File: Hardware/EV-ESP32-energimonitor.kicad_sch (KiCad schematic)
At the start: 0 parts

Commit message: HW added
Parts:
- added A1: ESP32_DevKit_V1_DOIT, Local_MCU_Module_Library:esp32_devkit_v1_doit (F.Mount), symbol Local_MCU_Module_Library:ESP32_DevKit_V1_DOIT
- added A2: DC-DC 3.3V 3A, Local_Misckllaneous_Library:DC-DC_3.3V_3A_Stepdown (F.Mount), symbol Local_Miscellaneous_Library:DC-DC_Step_Down_3.3V_3A
- added F1: Fuse, symbol Device:Fuse
- added J1: Conn_01x04_Socket, symbol Connector:Conn_01x04_Socket
- added PS1: RAC04-05SGA, Converter_ACDC:Converter_ACDC_RECOM_RAC04-xxSGx_THT, symbol Converter_ACDC:RAC04-05SGA
- added RV1: Varistor, symbol Device:Varistor

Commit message: HW: diagram added
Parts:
- removed J1: Conn_01x04_Socket, symbol Connector:Conn_01x04_Socket
- added C1, C7: C10uf, Capacitor_SMD:C_0603_1608Metric, symbol Local_Device_Library:C10uf
- added C2, C3, C4, C5, C6, C8: C100nf, Capacitor_SMD:C_0402_1005Metric, symbol Local_Device_Library:C100nf
- added C9: C, symbol Device:C
- added J2: Conn_01x02_Pin, symbol Connector:Conn_01x02_Pin
- added J3: RJ22, symbol Connector:RJ22
- added Q1: PNP, symbol Simulation_SPICE:PNP
- added Q2, Q3: NPN, symbol Simulation_SPICE:NPN
- added R1, R2: R10K, Resistor_SMD:R_0402_1005Metric, symbol Local_Device_Library:R10K
- added R3, R9: R, symbol Device:R
- added R4, R5, R6, R7, R8: R4.7K, Resistor_SMD:R_0402_1005Metric, symbol Local_Device_Library:R4.7K
- added SW1, SW2, SW3, SW4: SW_Push, symbol Switch:SW_Push
- added SW2: SW_MEC_5E, symbol Switch:SW_MEC_5E
- added U1: ER_OLEDM0.91_1x-I2C, Display:ER_OLEDM0.91_1x-I2C, symbol Display_Graphic:ER_OLEDM0.91_1x-I2C
- added U2: 74HC14, Package_SO:SOIC-14_3.9x8.7mm_P1.27mm, symbol Local_Miscellaneous_Library:74HC14-local_74HCxx
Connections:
- net at PS1.1 (AC(L)): now also F1.1, RV1.1
- net at PS1.2 (AC(N)): now also RV1.2
- net GND1: now reaches PS1.4 (-Vout)
- net GND1: now also A2.3 (IN-), C9.2, Q2.3 (E), Q3.3 (E), SW2.3 (K), SW2.4 (A)
- net at PS1.5 (+Vout): now also Q1.3 (E), R3.1, R9.1
- net at A2.2 (IN+): now also Q1.1 (C)
- net -3V3: now reaches A2.5 (OUT+)
- net -3V3: now also A1.16 (3V3), C3.1, C4.1, C5.1, C6.1, C7.1, C8.1, R1.1, R4.1, SW1.2, SW2.2, SW3.2, SW4.2, U1.2 (VCC)
- net GND: now reaches A2.8 (OUT-)
- net GND: now also A1.14 (GND), A1.17 (GND), C1.2, C2.2, C7.2, C8.2, J3.2, R2.2, R5.2, R6.2, R7.2, R8.2, U1.1 (GND)
- net at A1.10 (IO27_(pullup)): now also U2.10
- net at A1.11 (IO14_(pullup)): now also U2.4
- net at A1.26 (IO21): now also U1.4 (SDA)
- net at A1.29 (IO22): now also U1.3 (SCL)
- net at A1.4 (IO34_(no_pullup)): now also J2.1 (Pin_1)
- net at A1.7 (IO33): now also U2.2
- net at A1.8 (IO25_(pullup)): now also U2.6
- net at A1.9 (IO26_(pullup)): now also U2.8
- new net: Q1.2 (B), Q2.1 (C), R3.2
- new net: C5.2, R7.1, SW3.1, U2.9
- new net: C9.1, Q2.2 (B), Q3.1 (C), R9.2, SW2.1, SW2.2
- new net: C4.2, R6.1, SW2.1, U2.5
- new net: C1.1, J2.2 (Pin_2), R1.2, R2.1
- new net: C3.2, R5.1, SW1.1, U2.3
- new net: C2.1, J3.3, R4.2, U2.1
- new net: C6.2, R8.1, SW4.1, U2.11
- no-connect marks 0 -> 4
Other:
- note added: "Connect to open collector output"
- note added: "EV charging start/stop"
- note added: "Keep near ESP32 pin 16"
- note added: "SCT01-T10/50A current sensor"
- note added: "price-limit decrease"
- note added: "price-limit increase"
- note added: "smart charging on/off"
- moved on the sheet: A2, F1, PS1, RV1

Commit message: HW: buttons, display and reboot logic added
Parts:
- removed A2: DC-DC 3.3V 3A, Local_Misckllaneous_Library:DC-DC_3.3V_3A_Stepdown (F.Mount), symbol Local_Miscellaneous_Library:DC-DC_Step_Down_3.3V_3A
- removed Q1: PNP, symbol Simulation_SPICE:PNP
- removed Q2, Q3: NPN, symbol Simulation_SPICE:NPN
- removed R9: R, symbol Device:R
- added C1, C11: 100n, symbol Device:C
- added C10: C_Polarized, symbol Device:C_Polarized
- added C2: 100nf, Capacitor_SMD:C_0402_1005Metric, symbol Local_Device_Library:C10nf
- added C3: 1uF, symbol Device:C
- added C4: 47nf, Capacitor_SMD:C_0402_1005Metric, symbol Local_Device_Library:C10nf
- added C5: 10uF, symbol Device:C
- added D1, D2, D3, D4: 1N4148WS, Diode_SMD:D_SOD-323F, symbol Local_Diode_Library:1N4148WS
- added D1, D2: LED_0805_G, LED_SMD:LED_0805_2012Metric, symbol Local_Diode_Library:LED_0805_G
- added J1: Screw_Terminal_01x02, symbol Connector:Screw_Terminal_01x02
- added J4: Conn_01x01_Pin, symbol Connector:Conn_01x01_Pin
- added J5, J6, J7, J8: Conn_01x06_Pin, symbol Connector:Conn_01x06_Pin
- added Q1, Q11, Q8: BC547, Package_TO_SOT_THT:TO-92_Inline, symbol Transistor_BJT:BC547
- added Q10: AO3401A, Package_TO_SOT_SMD:SOT-23, symbol Transistor_FET:AO3401A
- added Q2: IRF4905, Package_TO_SOT_THT:TO-220-3_Vertical, symbol Transistor_FET:IRF4905
- added Q4, Q5, Q6, Q7: S8050_NPN, Package_TO_SOT_SMD:SOT-23, symbol Local_Transistor_BJT_Library:S8050_NPN
- added Q9: NPN, symbol Simulation_SPICE:NPN
- added R1: 47K, symbol Device:R
- added R10, R13: R180, Resistor_SMD:R_0805_2012Metric, symbol Local_Device_Library:R180
- added R11, R12: R10K, Resistor_SMD:R_0402_1005Metric, symbol Local_Device_Library:R10K
- added R19, R6: 2,2K, symbol Device:R
- added R2: 68K, symbol Device:R
- added R20, R4, R7 (x2): 100K, symbol Device:R
- added R23: R, symbol Device:R
- added R3: 220K, symbol Device:R
- added R5: 330K -> 390K, symbol Device:R
- added R6: R4.7K, Resistor_SMD:R_0402_1005Metric, symbol Local_Device_Library:R4.7K
- added unit 2 of U1
- added unit 3 of U1
- added U5: 74HC14, Package_SO:SOIC-14_3.9x8.7mm_P1.27mm, symbol Local_Miscellaneous_Library:74HC14-local_74HCxx
- C9: value C -> 1uF
- R3: value R -> 100K
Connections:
- net GND: now also C9.2, PS1.4 (-Vout), C1.2, C10.2, C11.2, C3.2, C5.2, D1.2 (A), D4.2 (A), J8.4 (Pin_4), Q1.3 (E), Q11.3 (E), Q4.2 (E), Q6.2 (E), Q8.3 (E), Q9.3 (E), R10.2, R13.2, R3.2, R4.2, R7.2, R7.2, U5.7 (GND); no longer U1.1 (GND)
- net GND1: now also U1.1 (GND), J7.4 (Pin_4); no longer C9.2, PS1.4 (-Vout)
- net at PS1.5 (+Vout), R3.1: now also D3.1 (K), Q2.3 (S), R1.1, R19.2, R2.1, R5.1
- net at R3.2: now also Q1.1 (C), Q2.1 (G)
- net at PS1.2 (AC(N)), RV1.2: now also J1.2 (Pin_2)
- net at C5.2, R7.1, U2.9: now also J6.3 (Pin_3); no longer SW3.1
- net at F1.2: now also J1.1 (Pin_1)
- net HARD_RESET_GPIO: now reaches A1.13 (IO13_(pullup))
- net HARD_RESET_GPIO: now also R23.1
- net VCC: now reaches A1.15 (VIN)
- net VCC: now also C10.1, Q2.2 (D)
- net ext. LED1: now reaches A1.19 (IO2_/_LED_PIN)
- net ext. LED1: now also R11.1
- net OLED Touch: now reaches A1.20 (IO4_(pullup))
- net OLED Touch: now also J6.5 (Pin_5)
- net ext. LED2: now reaches A1.21 (IO16)
- net ext. LED2: now also R12.1
- net at U1.4 (SDA): now also J7.3 (Pin_3); no longer A1.26 (IO21)
- net at U1.3 (SCL): now also J7.2 (Pin_2); no longer A1.29 (IO22)
- net Direct Reset GPIO: now reaches A1.6 (IO32)
- net Direct Reset GPIO: now also Q11.1 (C)
- net at SW2.1, SW2.2: now also J5.6 (Pin_6); no longer C9.1
- net at C4.2, R6.1, U2.5: now also J6.2 (Pin_2); no longer SW2.1
- net at C3.2, R5.1, U2.3: now also J6.1 (Pin_1); no longer SW1.1
- net at C6.2, R8.1, U2.11: now also J6.4 (Pin_4); no longer SW4.1
- net +3.3V: now reaches U2.14 (VCC)
- net +3.3V: now also A1.16 (3V3), C3.1, C4.1, C5.1, C6.1, C7.1, C8.1, R1.1, R4.1, J8.1 (Pin_1)
- removed net -3V3: A1.16 (3V3), C3.1, C4.1, C5.1, C6.1, C7.1, C8.1, R1.1, R4.1, SW1.2, SW2.2, SW3.2, SW4.2, U1.2 (VCC)
- new net: Q6.1 (B), Q7.2 (E), R13.1
- new net: Q8.2 (B), R6.1, R7.1
- new net: Q1.2 (B), R6.2, R7.1
- new net: Q4.1 (B), Q5.2 (E), R10.1
- new net: Q4.3 (C), Q5.1 (B), R11.2
- new net: J5.2 (Pin_2), SW2.1
- new net: Q11.2 (B), R19.1, R20.1
- new net: Q6.3 (C), Q7.1 (B), R12.2
- new net: J8.5 (Pin_5), Q5.3 (C)
- new net: J5.3 (Pin_3), SW3.1
- new net: J5.4 (Pin_4), SW4.1
- new net: C11.1, C9.1, U5.14 (VCC)
- new net: J5.1 (Pin_1), SW1.1
- new net: J8.6 (Pin_6), Q7.3 (C)
- new net: D2.1 (K), J7.6 (Pin_6)
- new net: D1.1 (K), J7.5 (Pin_5)
- new net: J4.1 (Pin_1), J5.5 (Pin_5)
- new net: Q9.2 (B), R23.2
- new net +3.3VA: D1.2 (A), D2.2 (A), J7.1 (Pin_1), SW1.2, SW2.2, SW3.2, SW4.2, U1.2 (VCC)
- new net BASE_H: R6.1, U5.12
- new net DLY_H: C4.2, U1.4
- new net EDGE_H: D2.2 (A), U1.2
- new net Kill Switch: C1.1, C2.2, J6.6 (Pin_6), Q9.1 (C), R1.2
- new net N250: C3.1, D2.1 (K), R3.1, U1.3
- new net N3S: C5.1, Q8.1 (C), R5.2, U5.11
- new net NSTART: C4.1, D3.2 (A), D4.1 (K), R4.1, U1.5
- new net NTRIG: C2.1, D1.1 (K), R2.2, U1.1
- new net OFF_WIN_H: U5.10, U5.13
- new net SCL: A1.29 (IO22), J8.2 (Pin_2)
- new net SDA: A1.26 (IO21), J8.3 (Pin_3)
- new net START_H: R6.2, U5.8
- new net START_N: R20.2, U1.6, U5.9
- no-connect marks 4 -> 0
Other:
- note added: "Capasitor sensor"
- note added: "Input - Internal Pullup Trigger on Falling adge"
- note added: "Keep close to Pin 14"
- note added: "en ny version specifikt med 74HC14"
- moved on the sheet: A1, C1, C2, C3, C4, C5, C6, C7, C8, F1, J2, J3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

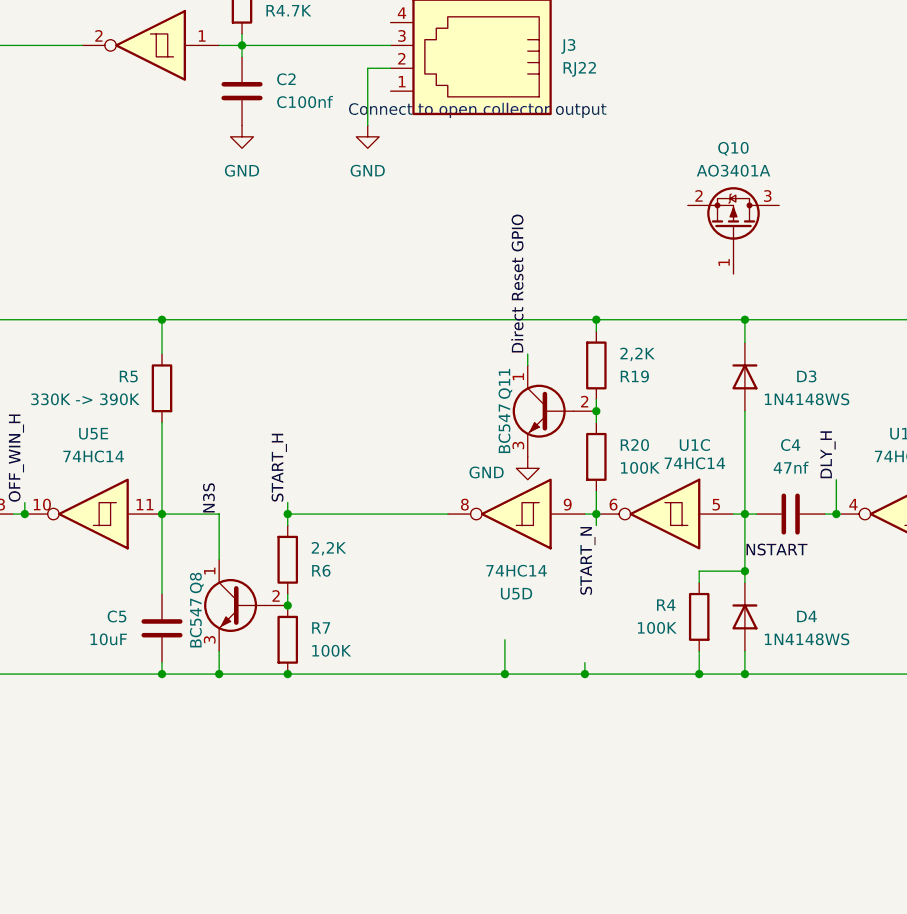
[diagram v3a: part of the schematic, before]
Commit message: FRM: #14 initial implementation. HW: Direct Reset GPIO Open Collector output added
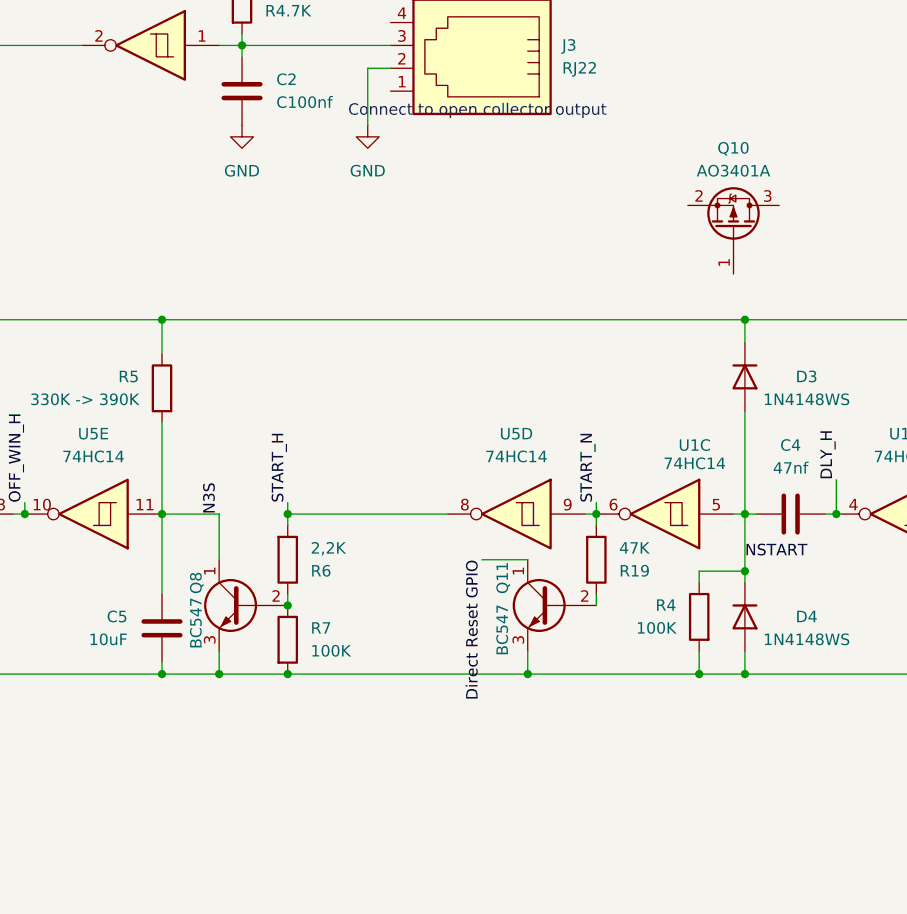
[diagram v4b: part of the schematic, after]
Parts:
- removed R20: 100K, symbol Device:R
- R19: value 2,2K -> 47K
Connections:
- net START_N: now also R19.2
- net at D3.1 (K), PS1.5 (+Vout), Q2.3 (S)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: no longer R19.2
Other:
- moved on the sheet: Q11, R19, U5D

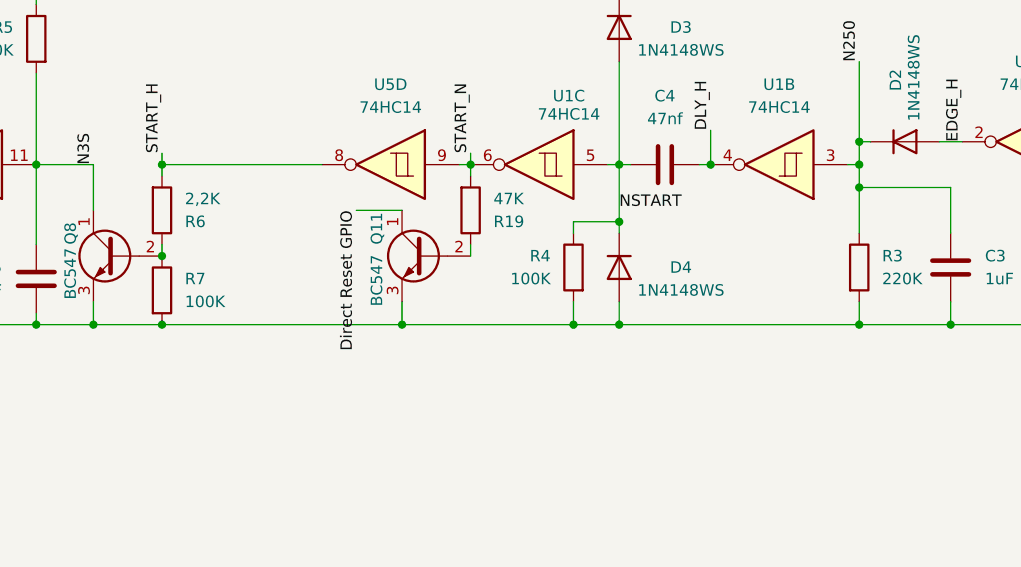
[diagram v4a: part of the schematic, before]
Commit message: HW: Direct Reset GPIO trigger moved to U1B pin 4
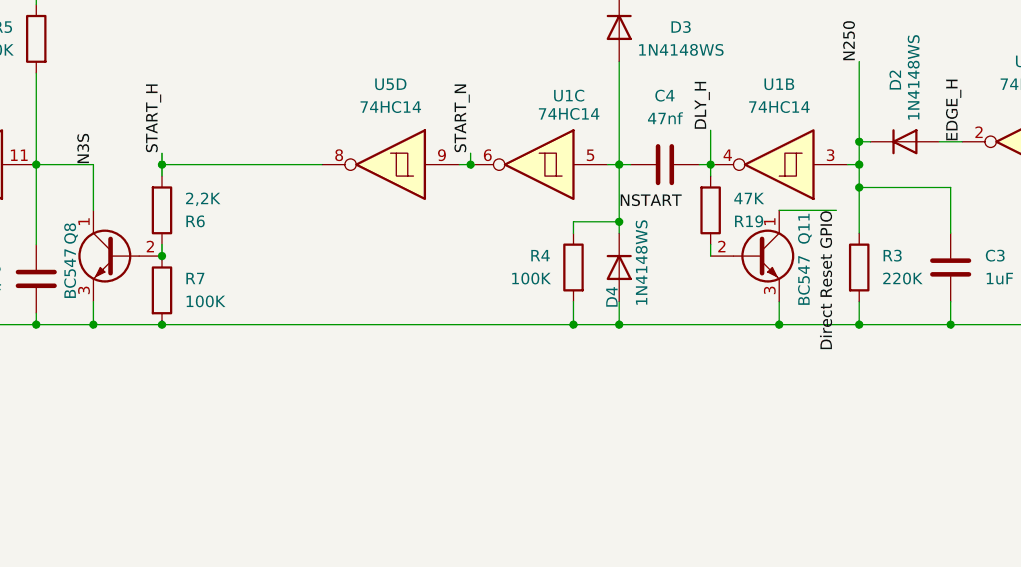
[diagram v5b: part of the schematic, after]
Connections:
- net DLY_H: now also R19.2
- net START_N: no longer R19.2
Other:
- moved on the sheet: Q11, R19
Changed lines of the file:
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@@
 	)
 	(junction
-		(at 213.36 232.41)
-		(diameter 0)
-		(color 0 0 0 0)
-	)
-	(junction
 		(at 341.63 146.05)
 		(diameter 0)
@@
 	)
 	(junction
+		(at 255.27 232.41)
+		(diameter 0)
+		(color 0 0 0 0)
+	)
+	(junction
 		(at 292.1 157.48)
 		(diameter 0)
@@
 	(wire
 		(pts
-			(xy 220.98 214.63) (xy 220.98 215.9)
-		)
-		(stroke
-			(width 0)
-			(type default)
-		)
-	)
-	(wire
-		(pts
 			(xy 52.07 186.69) (xy 52.07 189.23)
 		)
@@
 	(wire
 		(pts
-			(xy 220.98 223.52) (xy 220.98 224.79)
+			(xy 247.65 223.52) (xy 247.65 224.79)
 		)
 		(stroke
@@
 	(wire
 		(pts
-			(xy 208.28 219.71) (xy 213.36 219.71)
+			(xy 261.62 219.71) (xy 255.27 219.71)
 		)
 		(stroke
@@
 	(wire
 		(pts
-			(xy 213.36 232.41) (xy 232.41 232.41)
-		)
-		(stroke
-			(width 0)
-			(type default)
-		)
-	)
-	(wire
-		(pts
 			(xy 46.99 177.8) (xy 46.99 179.07)
 		)
@@
 	(wire
 		(pts
-			(xy 232.41 232.41) (xy 264.16 232.41)
+			(xy 232.41 232.41) (xy 255.27 232.41)
 		)
 		(stroke
@@
 	(wire
 		(pts
+			(xy 255.27 232.41) (xy 264.16 232.41)
+		)
+		(stroke
+			(width 0)
+			(type default)
+		)
+	)
+	(wire
+		(pts
 			(xy 303.53 209.55) (xy 306.07 209.55)
 		)
@@
 	(wire
 		(pts
-			(xy 90.17 57.15) (xy 102.87 57.15)
+			(xy 186.69 232.41) (xy 232.41 232.41)
 		)
 		(stroke
@@
 	(wire
 		(pts
-			(xy 353.06 212.09) (xy 367.03 212.09)
+			(xy 90.17 57.15) (xy 102.87 57.15)
 		)
 		(stroke
@@
 	(wire
 		(pts
-			(xy 332.74 156.21) (xy 341.63 156.21)
+			(xy 353.06 212.09) (xy 367.03 212.09)
 		)
 		(stroke
@@
 	(wire
 		(pts
-			(xy 261.62 123.19) (xy 261.62 129.54)
+			(xy 332.74 156.21) (xy 341.63 156.21)
 		)
 		(stroke
@@
 	(wire
 		(pts
-			(xy 254 124.46) (xy 254 123.19)
+			(xy 261.62 123.19) (xy 261.62 129.54)
 		)
 		(stroke
@@
 	(wire
 		(pts
-			(xy 293.37 193.04) (xy 351.79 193.04)
+			(xy 254 124.46) (xy 254 123.19)
 		)
 		(stroke
@@
 	(wire
 		(pts
-			(xy 237.49 214.63) (xy 238.76 214.63)
+			(xy 293.37 193.04) (xy 351.79 193.04)
 		)
 		(stroke
@@
 	(wire
 		(pts
-			(xy 213.36 229.87) (xy 213.36 232.41)
+			(xy 237.49 214.63) (xy 238.76 214.63)
 		)
 		(stroke
@@
 	(wire
 		(pts
+			(xy 247.65 214.63) (xy 247.65 215.9)
+		)
+		(stroke
+			(width 0)
+			(type default)
+		)
+	)
+	(wire
+		(pts
 			(xy 113.03 106.68) (xy 97.79 106.68)
 		)
@@
 	(wire
 		(pts
-			(xy 179.07 232.41) (xy 186.69 232.41)
+			(xy 255.27 229.87) (xy 255.27 232.41)
 		)
 		(stroke
@@
 	(wire
 		(pts
-			(xy 200.66 69.85) (xy 200.66 74.93)
+			(xy 179.07 232.41) (xy 186.69 232.41)
 		)
 		(stroke
@@
 	(wire
 		(pts
-			(xy 120.65 113.03) (xy 123.19 113.03)
+			(xy 200.66 69.85) (xy 200.66 74.93)
 		)
 		(stroke
@@
 	(wire
 		(pts
-			(xy 130.81 232.41) (xy 172.72 232.41)
+			(xy 120.65 113.03) (xy 123.19 113.03)
 		)
 		(stroke
@@
 	(wire
 		(pts
-			(xy 316.23 199.39) (xy 316.23 209.55)
+			(xy 130.81 232.41) (xy 172.72 232.41)
 		)
 		(stroke
@@
 	(wire
 		(pts
-			(xy 247.65 123.19) (xy 247.65 124.46)
+			(xy 316.23 199.39) (xy 316.23 209.55)
 		)
 		(stroke
@@
 	(wire
 		(pts
-			(xy 232.41 229.87) (xy 232.41 232.41)
+			(xy 247.65 123.19) (xy 247.65 124.46)
 		)
 		(stroke
@@
 	(wire
 		(pts
-			(xy 186.69 232.41) (xy 213.36 232.41)
+			(xy 232.41 229.87) (xy 232.41 232.41)
 		)
 		(stroke
@@
 	)
 	(label "Direct Reset GPIO"
-		(at 208.28 219.71 270)
+		(at 261.62 219.71 270)
 		(effects
 			(font
@@
 	(symbol
 		(lib_id "Device:R")
-		(at 220.98 219.71 0)
+		(at 247.65 219.71 0)
 		(mirror x)
 		(unit 1)
@@
 		(dnp no)
 		(property "Reference" "R19"
-			(at 223.52 220.9801 0)
+			(at 250.19 220.9801 0)
 			(show_name no)
 			(do_not_autoplace no)
@@
 		)
 		(property "Value" "47K"
-			(at 223.52 218.4401 0)
+			(at 250.19 218.4401 0)
 			(show_name no)
 			(do_not_autoplace no)
@@
 		)
 		(property "Footprint" ""
-			(at 219.202 219.71 90)
+			(at 245.872 219.71 90)
 			(hide yes)
 			(show_name no)
@@
 		)
 		(property "Datasheet" ""
-			(at 220.98 219.71 0)
+			(at 247.65 219.71 0)
 			(hide yes)
 			(show_name no)
@@
 		)
 		(property "Description" "Resistor"
-			(at 220.98 219.71 0)
+			(at 247.65 219.71 0)
 			(hide yes)
 			(show_name no)
@@
 		(dnp no)
 		(property "Reference" "D4"
-			(at 244.348 226.06 90)
+			(at 236.728 229.362 0)
 			(show_name no)
 			(do_not_autoplace no)
@@
 		)
 		(property "Value" "1N4148WS"
-			(at 244.348 228.6 90)
+			(at 240.03 225.552 0)
 			(show_name no)
 			(do_not_autoplace no)
@@
 	(symbol
 		(lib_id "Transistor_BJT:BC547")
-		(at 215.9 224.79 0)
-		(mirror y)
+		(at 252.73 224.79 0)
 		(unit 1)
 		(body_style 1)
@@
 		(dnp no)
 		(property "Reference" "Q11"
-			(at 210.566 223.52 90)
+			(at 258.064 223.52 90)
 			(show_name no)
 			(do_not_autoplace no)
@@
 		)
 		(property "Value" "BC547"
-			(at 210.566 230.378 90)
+			(at 258.064 230.378 90)
 			(show_name no)
 			(do_not_autoplace no)
@@
 		)
 		(property "Footprint" "Package_TO_SOT_THT:TO-92_Inline"
-			(at 210.82 226.695 0)
+			(at 257.81 226.695 0)
 			(hide yes)
 			(show_name no)
@@
 		)
 		(property "Datasheet" "https://www.onsemi.com/pub/Collateral/BC550-D.pdf"
-			(at 215.9 224.79 0)
+			(at 252.73 224.79 0)
 			(hide yes)
 			(show_name no)
@@
 		)
 		(property "Description" "0.1A Ic, 45V Vce, Small Signal NPN Transistor, TO-92"
-			(at 215.9 224.79 0)
+			(at 252.73 224.79 0)
 			(hide yes)
 			(show_name no)
@@
 		)
 		(property "Sim.Device" "NPN"
-			(at 215.9 224.79 0)
+			(at 252.73 224.79 0)
 			(hide yes)
 			(show_name no)
@@
 		)
 		(property "Sim.Pins" "1=C 2=B 3=E"
-			(at 215.9 224.79 0)
+			(at 252.73 224.79 0)
 			(hide yes)
 			(show_name no)

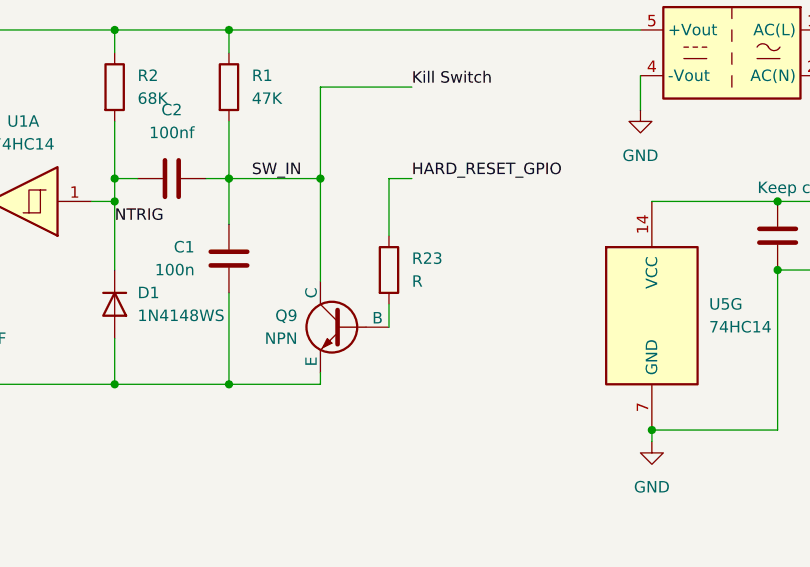
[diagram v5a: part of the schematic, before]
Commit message: FRM: HARD_RESET_GPIO change to Active HIGH and init. relocated. HW:  HARD_RESET_GPIO logic finalized
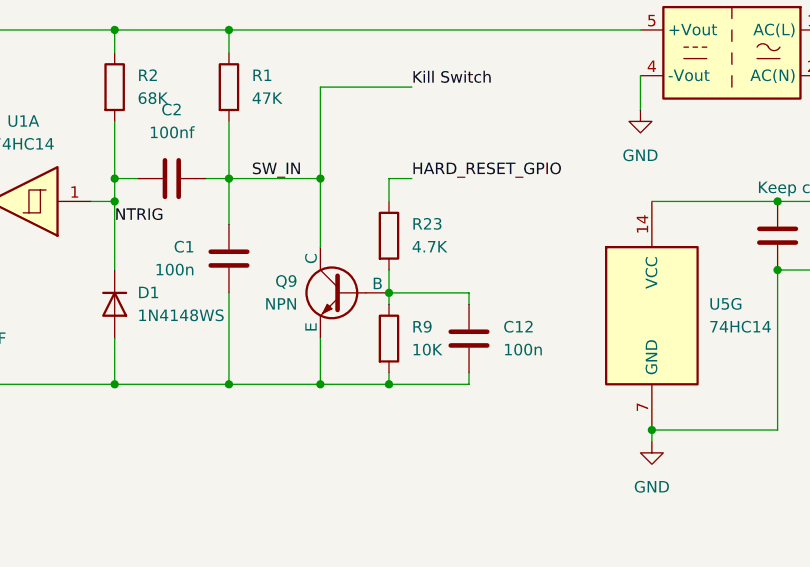
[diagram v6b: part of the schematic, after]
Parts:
- added C12: 100n, symbol Device:C
- added R9: 10K, symbol Device:R
- R23: value R -> 4.7K
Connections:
- net GND: now also C12.2, R9.2
- net at Q9.2 (B), R23.2: now also C12.1, R9.1
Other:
- moved on the sheet: Q9, R23
